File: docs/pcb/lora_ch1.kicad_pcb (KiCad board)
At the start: 2 copper layers, 6 parts, among them J1 JST_02, U1 ESP32-C3_SUPERMINI_TH, U2 TP4056-42-ESOP8, U3 DRV2605LDGS, U4 AP2112K-3.3

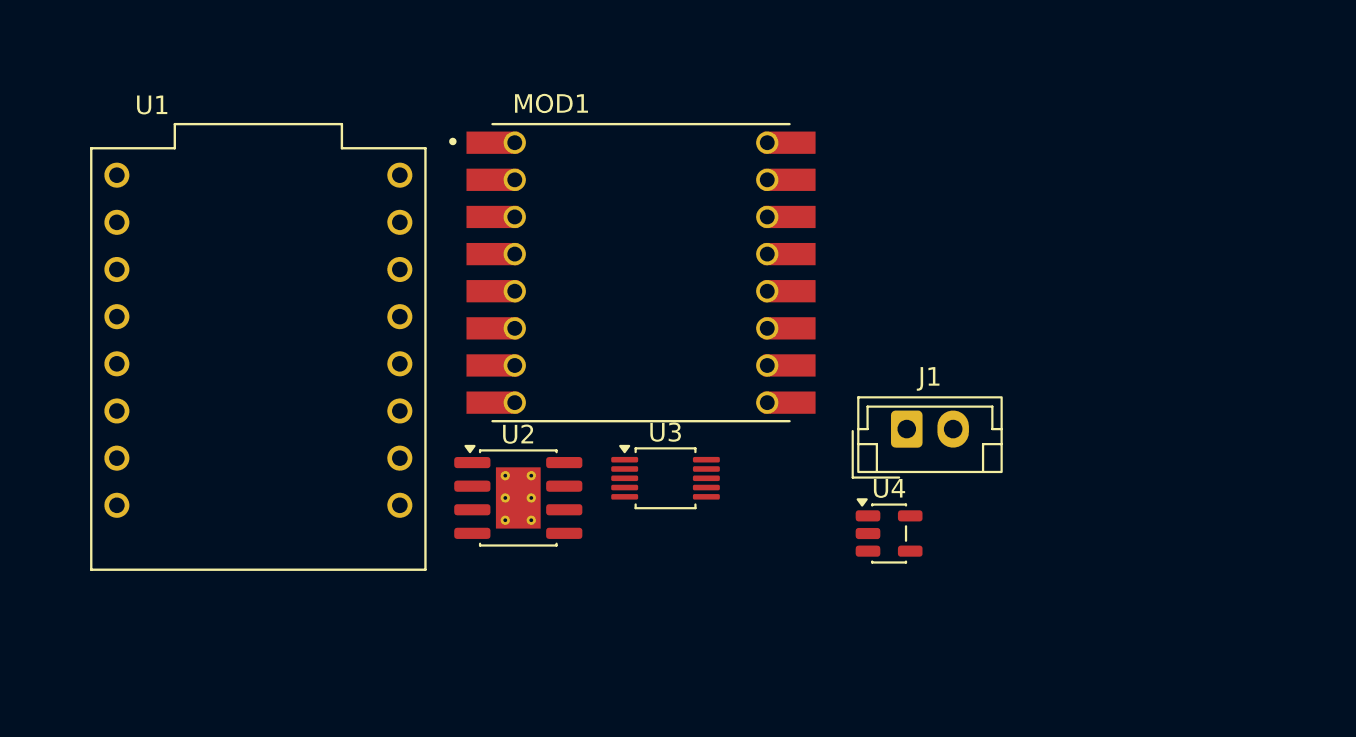
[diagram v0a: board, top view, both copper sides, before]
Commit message: PCB schematic update, charging function added.
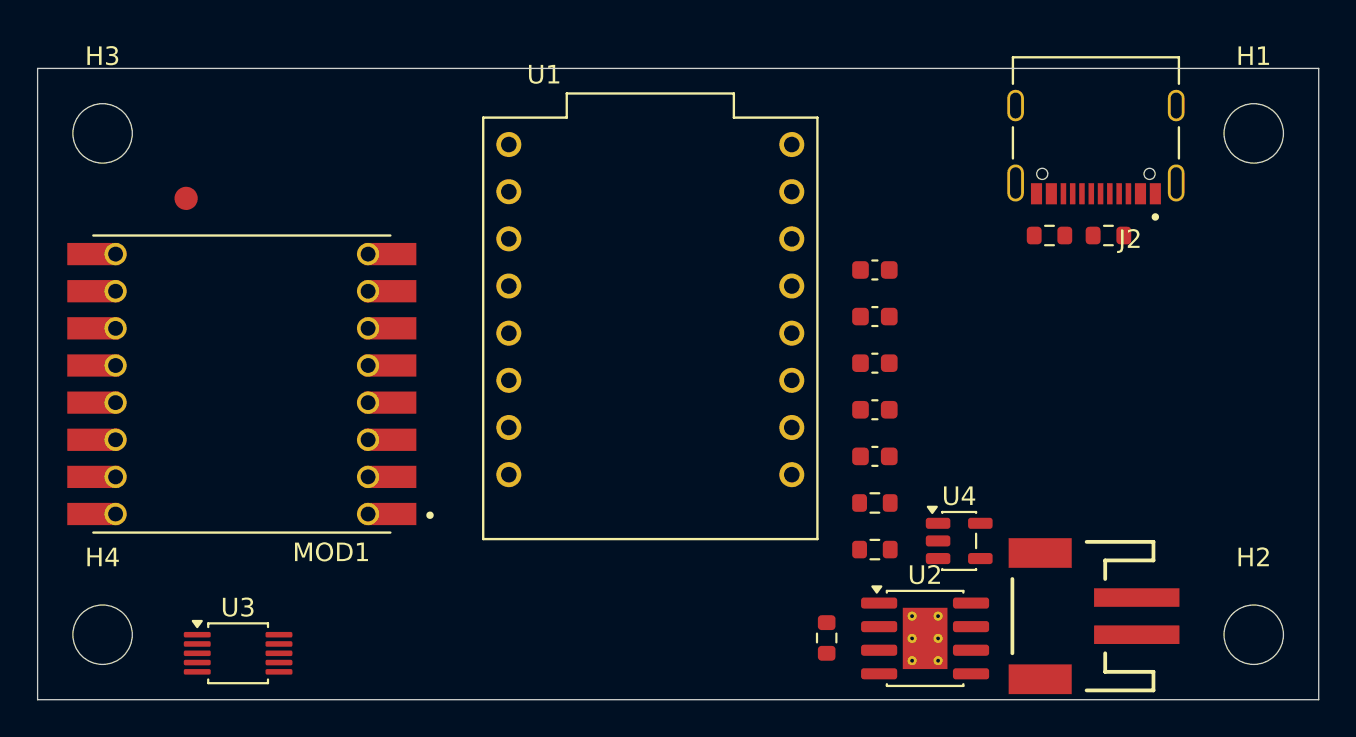
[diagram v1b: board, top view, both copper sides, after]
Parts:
- removed J1: JST_02, Connector_JST:JST_EH_B2B-EH-A_1x02_P2.50mm_Vertical
- added C1: 0.1uF, PCM_SparkFun-Capacitor:C_0603_1608Metric, F.Cu at (158.1, 93.9)
- added C2: 10uF, PCM_SparkFun-Capacitor:C_0603_1608Metric, F.Cu at (158.1, 96.4)
- added C3: 0.1uF, PCM_SparkFun-Capacitor:C_0603_1608Metric, F.Cu at (158.1, 98.9)
- added C4: 0.1uF, PCM_SparkFun-Capacitor:C_0603_1608Metric, F.Cu at (158.1, 101.4)
- added C5: 10uF, PCM_SparkFun-Capacitor:C_0603_1608Metric, F.Cu at (158.1, 103.9)
- added H1: MountingHole_M3, MountingHole:MountingHole_3.2mm_M3, F.Cu at (178.5, 86.5)
- added H2: MountingHole_M3, MountingHole:MountingHole_3.2mm_M3, F.Cu at (178.5, 113.5)
- added H3: MountingHole_M3, MountingHole:MountingHole_3.2mm_M3, F.Cu at (116.5, 86.5)
- added H4: MountingHole_M3, MountingHole:MountingHole_3.2mm_M3, F.Cu at (116.5, 113.5)
- added J2: TYPE-C-31-M-12, TYPE-C-31-M-12:HRO_TYPE-C-31-M-12, F.Cu at (170.0, 85.0)
- added J3: JST_2mm_LiPo, PCM_SparkFun-Connector:JST_1x02_P2.0mm_Horizontal_SMD, F.Cu at (168.5, 112.5)
- added R1: 2.0k, PCM_SparkFun-Resistor:R_0603_1608Metric, F.Cu at (155.5, 113.7)
- added R2: 5.1k, PCM_SparkFun-Resistor:R_0603_1608Metric, F.Cu at (167.5, 92.0)
- added R3: 5.1k, PCM_SparkFun-Resistor:R_0603_1608Metric, F.Cu at (170.7, 92.0)
- added R4: 4.7k, PCM_SparkFun-Resistor:R_0603_1608Metric, F.Cu at (158.1, 106.4)
- added R5: 4.7k, PCM_SparkFun-Resistor:R_0603_1608Metric, F.Cu at (158.1, 108.9)
- added TP1: 1.25mm, PCM_SparkFun-Connector:TestPoint-1.25mm, F.Cu at (121.0, 90.0)
- moved U3 24.9 mm to (123.8, 114.5)
- moved U2 23.2 mm to (160.8, 113.7)
- moved MOD1 22.3 mm to (124.0, 100.0), turned to 180 degrees
- moved U1 21.2 mm to (146.0, 97.0)
- moved U4 3.80 mm to (162.6, 108.5)
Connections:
- MOD1 pad 11: Net-(MOD1-DIO3-Pad11) -> unconnected-(MOD1-DIO3-Pad11)
- MOD1 pad 11_1: Net-(MOD1-DIO3-Pad11) -> unconnected-(MOD1-DIO3-Pad11)_1
- MOD1 pad 12: Net-(MOD1-DIO4-Pad12) -> unconnected-(MOD1-DIO4-Pad12)
- MOD1 pad 12_1: Net-(MOD1-DIO4-Pad12) -> unconnected-(MOD1-DIO4-Pad12)_1
- MOD1 pad 14: Net-(MOD1-DIO0-Pad14) -> DIO0
- MOD1 pad 14_1: Net-(MOD1-DIO0-Pad14) -> DIO0
- MOD1 pad 15: Net-(MOD1-DIO1-Pad15) -> unconnected-(MOD1-DIO1-Pad15)_1
- MOD1 pad 15_1: Net-(MOD1-DIO1-Pad15) -> unconnected-(MOD1-DIO1-Pad15)
- MOD1 pad 16: Net-(MOD1-DIO2-Pad16) -> unconnected-(MOD1-DIO2-Pad16)
- MOD1 pad 16_1: Net-(MOD1-DIO2-Pad16) -> unconnected-(MOD1-DIO2-Pad16)_1
- MOD1 pad 2: Net-(MOD1-MISO-Pad2) -> MISO
- MOD1 pad 2_1: Net-(MOD1-MISO-Pad2) -> MISO
- MOD1 pad 3: Net-(MOD1-MOSI-Pad3) -> MOSI
- MOD1 pad 3_1: Net-(MOD1-MOSI-Pad3) -> MOSI
- MOD1 pad 4: Net-(MOD1-SCK-Pad4) -> SCK
- MOD1 pad 4_1: Net-(MOD1-SCK-Pad4) -> SCK
- MOD1 pad 5: Net-(MOD1-NSS-Pad5) -> NSS
- MOD1 pad 5_1: Net-(MOD1-NSS-Pad5) -> NSS
- MOD1 pad 6: Net-(MOD1-RESET-Pad6) -> RESET
- MOD1 pad 6_1: Net-(MOD1-RESET-Pad6) -> RESET
- MOD1 pad 7: Net-(MOD1-DIO5-Pad7) -> unconnected-(MOD1-DIO5-Pad7)_1
- MOD1 pad 7_1: Net-(MOD1-DIO5-Pad7) -> unconnected-(MOD1-DIO5-Pad7)
- U1 pad 2: unconnected-(U1-GPIO2-Pad2) -> DIO0
- U1 pad 3: unconnected-(U1-GPIO3-Pad3) -> RESET
- U1 pad 3.3: unconnected-(U1-3V3-Pad3.3) -> +3.3V
- U1 pad 4: unconnected-(U1-GPIO4-Pad4) -> SCK
- U1 pad 5: unconnected-(U1-GPIO5-Pad5) -> MISO
- U1 pad 6: unconnected-(U1-GPIO6-Pad6) -> MOSI
- U1 pad 7: unconnected-(U1-GPIO7-Pad7) -> NSS
- U1 pad 8: unconnected-(U1-GPIO8-Pad8) -> SDA
- U1 pad 9: unconnected-(U1-GPIO9-Pad9) -> SCL
- U1 pad G: unconnected-(U1-GND-PadG) -> GND
- U2 pad 1: unconnected-(U2-TEMP-Pad1) -> GND
- U2 pad 2: unconnected-(U2-PROG-Pad2) -> Net-(U2-PROG)
- U2 pad 3: unconnected-(U2-GND-Pad3) -> GND
- U2 pad 4: unconnected-(U2-V_{CC}-Pad4) -> TYPE_C_VCC
- U2 pad 5: unconnected-(U2-BAT-Pad5) -> Net-(J3-+)
- U2 pad 8: unconnected-(U2-CE-Pad8) -> TYPE_C_VCC
- U2 pad 9: unconnected-(U2-EPAD-Pad9) -> GND
- U3 pad 1: unconnected-(U3-REG-Pad1) -> Net-(U3-REG)
- U3 pad 10: unconnected-(U3-VDD-Pad10) -> Net-(U3-VDD)
- U3 pad 2: unconnected-(U3-SCL-Pad2) -> SCL
- U3 pad 3: unconnected-(U3-SDA-Pad3) -> SDA
- U3 pad 5: unconnected-(U3-EN-Pad5) -> +3.3V
- U3 pad 6: unconnected-(U3-VDD/NC-Pad6) -> +3.3V
- U3 pad 8: unconnected-(U3-GND-Pad8) -> GND
- U4 pad 1: unconnected-(U4-VIN-Pad1) -> Net-(J3-+)
- U4 pad 2: unconnected-(U4-GND-Pad2) -> GND
- U4 pad 3: unconnected-(U4-EN-Pad3) -> Net-(J3-+)
- U4 pad 5: unconnected-(U4-VOUT-Pad5) -> +3.3V
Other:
- board outline added: 69 x 34 mm

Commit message: PCB schematic finished.
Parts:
- removed H1, H2, H3, H4: MountingHole_M3, MountingHole:MountingHole_3.2mm_M3
- removed J2: TYPE-C-31-M-12, TYPE-C-31-M-12:HRO_TYPE-C-31-M-12
- removed J3: JST_2mm_LiPo, PCM_SparkFun-Connector:JST_1x02_P2.0mm_Horizontal_SMD
- removed MOD1: RFM98W-433S2, RFM98W-433S2:XCVR_RFM98W-433S2
- removed R3: 5.1k, PCM_SparkFun-Resistor:R_0603_1608Metric
- removed TP1: 1.25mm, PCM_SparkFun-Connector:TestPoint-1.25mm
- removed U1: ESP32-C3_SUPERMINI_TH, ESP32-C3_SUPERMINI_TH:MODULE_ESP32-C3_SUPERMINI_TH
- removed U2: TP4056-42-ESOP8, Package_SO:SOIC-8-1EP_3.9x4.9mm_P1.27mm_EP2.41x3.3mm_ThermalVias
- removed U3: DRV2605LDGS, Package_SO:VSSOP-10_3x3mm_P0.5mm
- removed U4: AP2112K-3.3, Package_TO_SOT_SMD:SOT-23-5
- added 3.3V_LDO1: XC6220B331MR, Package_TO_SOT_SMD:SOT-23-5, F.Cu at (122.4, 75.5)
- added ANT_PAD1: PINHD_1x1_Male, Connector_Pin:Pin_D1.0mm_L10.0mm_LooseFit, F.Cu at (82.5, 67.0)
- added BATT_CON1: JST_2mm_LiPo, PCM_SparkFun-Connector:JST_1x02_P2.0mm_Horizontal_SMD, F.Cu at (130.5, 90.0)
- added BATT_PROT1: DW01A, Package_TO_SOT_SMD:SOT-23-6, F.Cu at (125.6, 66.5)
- added BATT_SD1: SS14, Diode_SMD:D_SMA, F.Cu at (132.0, 83.0)
- added BMS_FET1: FS8205A, FS8205A:SOP65P640X120-8N, F.Cu at (124.0, 62.5)
- added C6: 100uF, PCM_SparkFun-Capacitor:C_1206_3216Metric, F.Cu at (138.5, 78.5)
- added C7: 100nF, PCM_SparkFun-Capacitor:C_0603_1608Metric, F.Cu at (134.3, 69.5)
- added C8: 1.0uF, PCM_SparkFun-Capacitor:C_0603_1608Metric, F.Cu at (134.3, 72.0)
- added CHRG_MOD1: TP4056-42-ESOP8, Package_SO:SOIC-8-1EP_3.9x4.9mm_P1.27mm_EP2.41x3.3mm_ThermalVias, F.Cu at (132.8, 63.2)
- added ESP32-C3-SUPERMINI1: ESP32-C3_SUPERMINI_TH, ESP32-C3_SUPERMINI_TH:MODULE_ESP32-C3_SUPERMINI_TH, F.Cu at (109.0, 71.5)
- added LORA_MOD1: RFM98W-433S2, RFM98W-433S2:XCVR_RFM98W-433S2, F.Cu at (86.5, 78.0)
- added LRA+1: PINHD_1x1_Male, Connector_Pin:Pin_D1.0mm_L10.0mm_LooseFit, F.Cu at (120.0, 91.0)
- added LRA-1: PINHD_1x1_Male, Connector_Pin:Pin_D1.0mm_L10.0mm_LooseFit, F.Cu at (124.0, 91.0)
- added LRA_DRV1: DRV2605LDGS, Package_SO:VSSOP-10_3x3mm_P0.5mm, F.Cu at (123.5, 81.5)
- added MOUNT1: MountingHole_M3, MountingHole:MountingHole_3.2mm_M3, F.Cu at (78.5, 63.5)
- added MOUNT2: MountingHole_M3, MountingHole:MountingHole_3.2mm_M3, F.Cu at (140.5, 63.5)
- added MOUNT3: MountingHole_M3, MountingHole:MountingHole_3.2mm_M3, F.Cu at (78.5, 91.0)
- added MOUNT4: MountingHole_M3, MountingHole:MountingHole_3.2mm_M3, F.Cu at (140.5, 91.0)
- added R6: 100, PCM_SparkFun-Resistor:R_0603_1608Metric, F.Cu at (138.3, 72.0)
- added R7: 1k, PCM_SparkFun-Resistor:R_0603_1608Metric, F.Cu at (138.3, 74.5)
- added TEST1: PINHD_1x6_Male, Connector_PinHeader_2.54mm:PinHeader_1x06_P2.54mm_Vertical, F.Cu at (102.4, 91.5)
- added USB_SD1: SS14, Diode_SMD:D_SMA, F.Cu at (123.5, 71.0)
- C1, C3, C4: value 0.1uF -> 10uF
- moved R1 44.5 mm to (134.3, 74.5), turned to 0 degrees
- moved R5 44.1 mm to (138.3, 69.5)
- moved C1 37.0 mm to (130.3, 69.5)
- moved C2 37.0 mm to (130.3, 72.0)
- moved C3 37.0 mm to (130.3, 74.5)
- moved C4 37.0 mm to (130.3, 77.0)
- moved C5 37.0 mm to (130.3, 79.5)
- moved R2 36.4 mm to (134.3, 77.0)
- moved R4 35.9 mm to (134.3, 79.5)
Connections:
- C1 pad 1: Net-(U3-VDD) -> GND
- C1 pad 2: GND -> 3.3V
- C2 pad 1: +3.3V -> GND
- C2 pad 2: GND -> V_IN
- C3 pad 2: Net-(U3-REG) -> V_USB
- C4 pad 1: +3.3V -> VBAT+
- C5 pad 1: 3.3V -> GND
- C5 pad 2: +3.3V -> V_IN
- R1 pad 1: Net-(U2-PROG) -> GND
- R1 pad 2: GND -> Net-(CHRG_MOD1-PROG)
- R2 pad 1: GND -> 3.3V
- R2 pad 2: Net-(J2-CC1) -> LORA_NSS
- R4 pad 1: +3.3V -> SDA
- R4 pad 2: SDA -> 3.3V
- R5 pad 1: SCL -> 3.3V
- R5 pad 2: +3.3V -> SCL
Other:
- board size 69 x 34 mm -> 69 x 34.5 mm

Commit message: PCB design finished.
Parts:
- removed 3.3V_LDO1: XC6220B331MR, Package_TO_SOT_SMD:SOT-23-5
- removed BATT_SD1, USB_SD1: SS14, Diode_SMD:D_SMA
- removed BMS_FET1: FS8205A, FS8205A:SOP65P640X120-8N
- removed TEST1: PINHD_1x6_Male, Connector_PinHeader_2.54mm:PinHeader_1x06_P2.54mm_Vertical
- added BMS: FS8205A, FS8205A:SOP65P640X120-8N, F.Cu at (121.9, 91.0)
- added C10: 0.1uF, PCM_SparkFun-Capacitor:C_0603_1608Metric, F.Cu at (117.7, 79.5)
- added C11: 0.1uF, PCM_SparkFun-Capacitor:C_0603_1608Metric, F.Cu at (137.5, 73.0)
- added C9: 0.1uF, PCM_SparkFun-Capacitor:C_0603_1608Metric, F.Cu at (128.0, 82.0)
- added DIO0: PINHD_1x6_Male, Connector_PinHeader_2.54mm:PinHeader_1x06_P2.54mm_Vertical, F.Cu at (112.2, 91.5)
- added INPT_BTN1: Push_Button, Button_Switch_THT:SW_PUSH_6mm, F.Cu at (87.2, 63.8)
- added LDO: XC6220B331MR, Package_TO_SOT_SMD:SOT-23-5, F.Cu at (119.5, 67.5)
- added MOSFET1: AO3401A, Package_TO_SOT_SMD:SOT-23, F.Cu at (123.5, 76.0)
- added R10: 100k, PCM_SparkFun-Resistor:R_0603_1608Metric, F.Cu at (125.5, 71.5)
- added R11: 100k, PCM_SparkFun-Resistor:R_0603_1608Metric, F.Cu at (132.0, 81.5)
- added R12: 10k, PCM_SparkFun-Resistor:R_0603_1608Metric, F.Cu at (100.7, 85.5)
- added R3: 100k, PCM_SparkFun-Resistor:R_0603_1608Metric, F.Cu at (117.5, 76.0)
- added R8: 100k, PCM_SparkFun-Resistor:R_0603_1608Metric, F.Cu at (123.0, 79.5)
- added R9: 10k, PCM_SparkFun-Resistor:R_0603_1608Metric, F.Cu at (120.8, 71.0)
- added SSD1: SS14, Diode_SMD:D_SMA, F.Cu at (119.5, 62.5)
- moved C1 51.0 mm to (83.0, 88.5), turned to 180 degrees
- moved R2 37.3 mm to (98.0, 85.5), turned to 90 degrees
- moved LRA+1 25.1 mm to (141.5, 78.0), turned to 90 degrees
- moved LRA-1 24.4 mm to (141.5, 74.0)
- moved BATT_PROT1 19.3 mm to (122.0, 85.5), turned to -90 degrees
- moved R7 18.9 mm to (121.0, 82.0), turned to 180 degrees
- moved C6 18.2 mm to (124.0, 67.5), turned to -90 degrees
- moved R6 18.0 mm to (127.0, 86.0), turned to 90 degrees
- moved C5 17.2 mm to (125.5, 63.0), turned to 180 degrees
- moved C7 15.8 mm to (119.0, 73.5)
- moved C4 14.5 mm to (134.0, 63.0)
- moved R5 13.5 mm to (127.5, 77.5)
- moved C3 11.5 mm to (129.7, 63.0)
- moved LRA_DRV1 11.4 mm to (134.0, 77.0), turned to 0 degrees
- moved C2 11.2 mm to (137.0, 81.0), turned to 180 degrees
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- renumbered ANT_PAD1 to ANT, LORA_MOD1 to RFM98W
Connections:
- net VBAT+ renamed BATT_PLUS
- net VBAT- renamed BATT_MINUS
- CHRG_MOD1 pad 7: unconnected-(CHRG_MOD1-~{CHRG}-Pad7) -> CHRG
- CHRG_MOD1 pad 9: unconnected-(CHRG_MOD1-EPAD-Pad9) -> GND
- ESP32-C3-SUPERMINI1 pad 0: unconnected-(ESP32-C3-SUPERMINI1-GPIO0-Pad0) -> Net-(ESP32-C3-SUPERMINI1-GPIO0)
- ESP32-C3-SUPERMINI1 pad 1: unconnected-(ESP32-C3-SUPERMINI1-GPIO1-Pad1) -> Net-(ESP32-C3-SUPERMINI1-GPIO1)
- ESP32-C3-SUPERMINI1 pad 10: unconnected-(ESP32-C3-SUPERMINI1-GPIO10-Pad10) -> LORA_DIO0
- ESP32-C3-SUPERMINI1 pad 2: LORA_DIO0 -> unconnected-(ESP32-C3-SUPERMINI1-GPIO2-Pad2)
- ESP32-C3-SUPERMINI1 pad 20: unconnected-(ESP32-C3-SUPERMINI1-GPIO20-Pad20) -> CHRG
- ESP32-C3-SUPERMINI1 pad 21: unconnected-(ESP32-C3-SUPERMINI1-GPIO21-Pad21) -> DRV_EN
- LRA_DRV1 pad 5: 3.3V -> DRV_EN
- RFM98W pad 11: Net-(LORA_MOD1-DIO3-Pad11) -> unconnected-(LORA_MOD1-DIO3-Pad11)
- RFM98W pad 11_1: Net-(LORA_MOD1-DIO3-Pad11) -> unconnected-(LORA_MOD1-DIO3-Pad11)_1
- RFM98W pad 12: Net-(LORA_MOD1-DIO4-Pad12) -> unconnected-(LORA_MOD1-DIO4-Pad12)
- RFM98W pad 12_1: Net-(LORA_MOD1-DIO4-Pad12) -> unconnected-(LORA_MOD1-DIO4-Pad12)_1
- RFM98W pad 15: Net-(LORA_MOD1-DIO1-Pad15) -> unconnected-(LORA_MOD1-DIO1-Pad15)_1
- RFM98W pad 15_1: Net-(LORA_MOD1-DIO1-Pad15) -> unconnected-(LORA_MOD1-DIO1-Pad15)
- RFM98W pad 16: Net-(LORA_MOD1-DIO2-Pad16) -> unconnected-(LORA_MOD1-DIO2-Pad16)
- RFM98W pad 16_1: Net-(LORA_MOD1-DIO2-Pad16) -> unconnected-(LORA_MOD1-DIO2-Pad16)_1
- RFM98W pad 7: Net-(LORA_MOD1-DIO5-Pad7) -> unconnected-(LORA_MOD1-DIO5-Pad7)_1
- RFM98W pad 7_1: Net-(LORA_MOD1-DIO5-Pad7) -> unconnected-(LORA_MOD1-DIO5-Pad7)
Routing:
- net 3.3V: track 0.00 -> 91.6 mm, vias 0 -> 3
- net V_IN: track 0.00 -> 82.0 mm, vias 0 -> 5
- net GND: track 0.00 -> 67.2 mm, vias 0 -> 10
- net SCL: track 0.00 -> 61.0 mm, vias 0 -> 3
- net SDA: track 0.00 -> 59.4 mm, vias 0 -> 4
- net DRV_EN: track 0.00 -> 55.4 mm, vias 0 -> 2
- net CHRG: track 0.00 -> 48.3 mm, vias 0 -> 5
- net V_USB: track 0.00 -> 47.5 mm
- net LORA_DIO0: track 0.00 -> 45.2 mm, vias 0 -> 2
- net BATT_PLUS: track 0.00 -> 41.6 mm, vias 0 -> 2
- net Net-(ESP32-C3-SUPERMINI1-GPIO1): track 0.00 -> 31.4 mm, vias 0 -> 1
- net LORA_MISO: track 0.00 -> 28.7 mm, vias 0 -> 1
- net LORA_NSS: track 0.00 -> 27.5 mm, vias 0 -> 1
- net LORA_SCK: track 0.00 -> 26.5 mm, vias 0 -> 1
- net BATT_MINUS: track 0.00 -> 26.4 mm
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- added copper zone on B.Cu, net GND
- added copper zone on F.Cu, net GND
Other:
- rule pad_to_mask_clearance: 0 -> 0.02
- board text added: "DIO0 VIN 3.3V SDA SCL GND"

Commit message: PCB ready to print.
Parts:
- removed ESP32-C3-SUPERMINI1: ESP32-C3_SUPERMINI_TH, ESP32-C3_SUPERMINI_TH:MODULE_ESP32-C3_SUPERMINI_TH
- added ESP1: ESP32-C3_SUPERMINI_SMD, ESP32-C3_SUPERMINI_SMD:MODULE_ESP32-C3_SUPERMINI, F.Cu at (106.0, 71.5)
- moved R3 1.41 mm to (118.5, 77.0)
- moved C10 0.78 mm to (118.5, 79.5)
- moved LORA1 0.50 mm to (86.0, 79.0)
- moved SSD1 0.50 mm to (120.0, 62.5)
- renumbered ANT to ANT1, BATT_CON1 to BATTC1, BATT_PROT1 to BATTP1, BMS to BMS1, CHRG_MOD1 to CHRG1, LRA_DRV1 to HAPTIC1, LDO to LDO1, RFM98W to LORA1, LRA-1 to LRAM1, LRA+1 to LRAP1, DIO0 to TEST1
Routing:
- net LORA_DIO0: track 45.2 -> 67.3 mm, vias 2 -> 4
- net GND: track 67.2 -> 54.6 mm, vias 10 -> 11
- net 3.3V: track 91.6 -> 93.8 mm, vias 3 -> 4
- net SCL: track 61.0 -> 62.7 mm, vias 3 -> 4
- net LORA_MOSI: track 24.3 -> 25.8 mm, vias 1 -> 2
- net CHRG: track 48.3 -> 49.8 mm, vias 5 -> 4
- net LORA_NSS: track 27.5 -> 28.8 mm, vias 1 -> 2
- net LORA_MISO: track 28.7 -> 29.8 mm, vias 1 -> 2
- net Net-(ESP1-GPIO0): track 12.5 -> 11.8 mm
- net SDA: track 59.4 -> 60.0 mm
- net LORA_RST: track 22.6 -> 22.9 mm, vias 0 -> 2
- net LORA_SCK: track 26.5 -> 26.6 mm, vias 1 -> 2
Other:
- board text added: "+"
- board text added: "-"
- board text added: "JLCJLCJLCJLC"
